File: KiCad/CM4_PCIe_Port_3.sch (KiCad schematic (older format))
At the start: 3 parts, among them J15 PCIe_x16

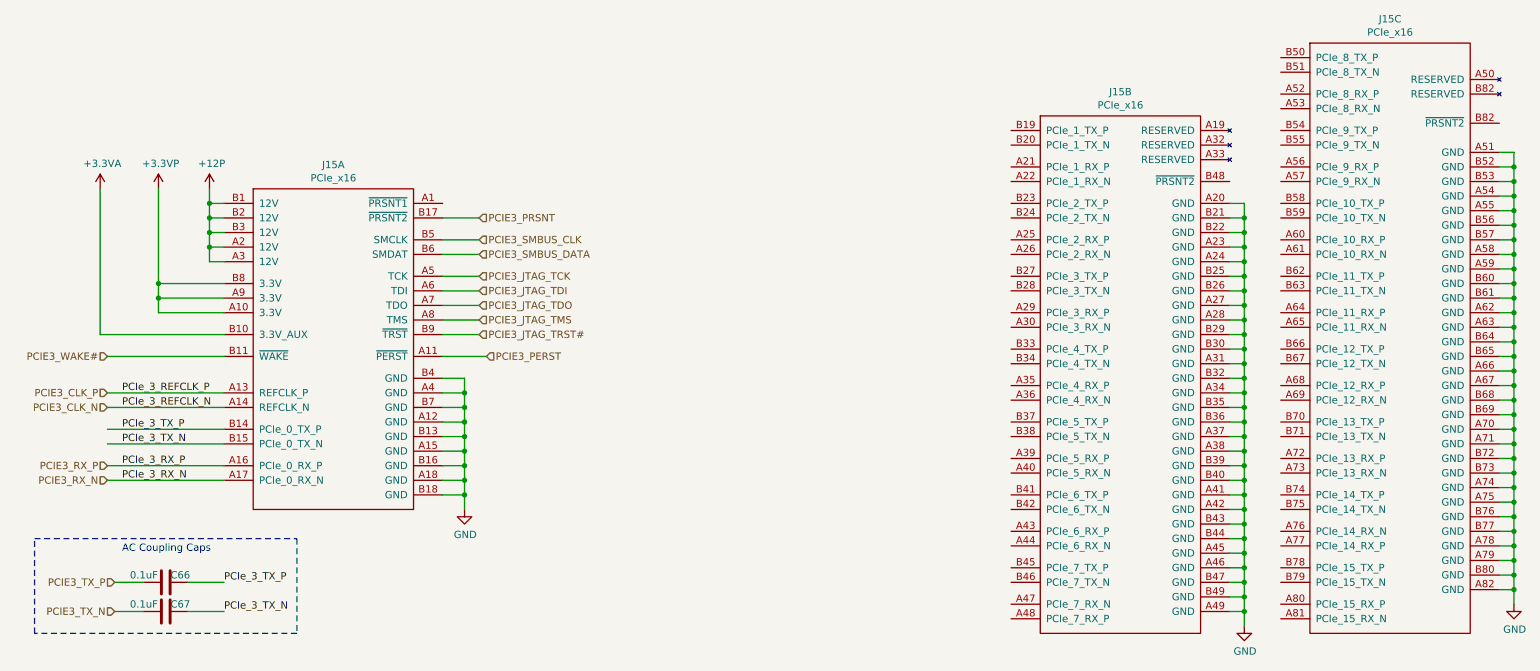
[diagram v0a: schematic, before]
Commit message: Tons of wiring and pin straps for PCI-e Switch
Also re-did some hierarchical labels for JTAG
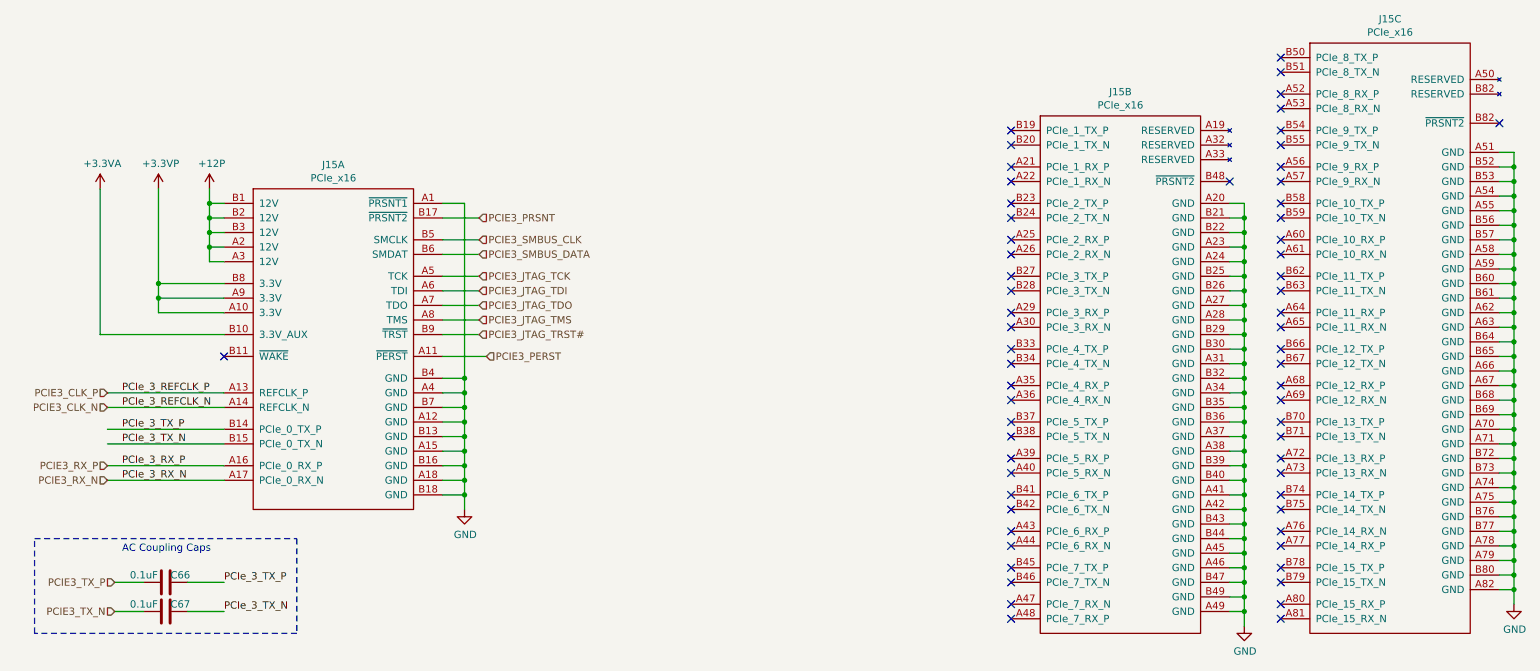
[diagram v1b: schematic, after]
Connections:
- net GND: now also J15.A1 (~PRSNT1)
- net PCIE3_WAKE#: no longer names the net of J15.B11 (~WAKE)
- no-connect marks 0 -> 63
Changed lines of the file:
@@
 PCIE3_SMBUS_DATA
-Wire Wire Line
-	2100 3700 1300 3700
-Text HLabel 1300 3700 0    50   Input ~ 0
-PCIE3_WAKE#
 Wire Wire Line
 	3600 3150 3850 3150
@@
 Text HLabel 3850 3550 2    50   Input ~ 0
 PCIE3_JTAG_TRST#
+NoConn ~ 9000 2500
+NoConn ~ 10850 2100
+NoConn ~ 9350 1650
+NoConn ~ 9350 1750
+NoConn ~ 9350 1900
+NoConn ~ 9350 2000
+NoConn ~ 9350 2150
+NoConn ~ 9350 2250
+NoConn ~ 9350 2400
+NoConn ~ 9350 2500
+NoConn ~ 9350 2650
+NoConn ~ 9350 2750
+NoConn ~ 9350 2900
+NoConn ~ 9350 3000
+NoConn ~ 9350 3150
+NoConn ~ 9350 3250
+NoConn ~ 9350 3400
+NoConn ~ 9350 3500
+NoConn ~ 9350 3650
+NoConn ~ 9350 3750
+NoConn ~ 9350 3900
+NoConn ~ 9350 4000
+NoConn ~ 9350 4150
+NoConn ~ 9350 4250
+NoConn ~ 9350 4400
+NoConn ~ 9350 4500
+NoConn ~ 9350 4650
+NoConn ~ 9350 4750
+NoConn ~ 9350 4900
+NoConn ~ 9350 5000
+NoConn ~ 9350 5150
+NoConn ~ 9350 5250
+NoConn ~ 9350 5400
+NoConn ~ 9350 5500
+NoConn ~ 7500 5500
+NoConn ~ 7500 5400
+NoConn ~ 7500 5250
+NoConn ~ 7500 5150
+NoConn ~ 7500 5000
+NoConn ~ 7500 4900
+NoConn ~ 7500 4750
+NoConn ~ 7500 4650
+NoConn ~ 7500 4500
+NoConn ~ 7500 4400
+NoConn ~ 7500 4250
+NoConn ~ 7500 4150
+NoConn ~ 7500 4000
+NoConn ~ 7500 3900
+NoConn ~ 7500 3750
+NoConn ~ 7500 3650
+NoConn ~ 7500 3500
+NoConn ~ 7500 3400
+NoConn ~ 7500 3250
+NoConn ~ 7500 3150
+NoConn ~ 7500 3000
+NoConn ~ 7500 2900
+NoConn ~ 7500 2750
+NoConn ~ 7500 2650
+NoConn ~ 7500 2500
+NoConn ~ 7500 2400
+NoConn ~ 7500 2250
+NoConn ~ 7500 2150
+Wire Wire Line
+	3600 2650 3750 2650
+Wire Wire Line
+	3750 2650 3750 3850
+Connection ~ 3750 3850
+NoConn ~ 2100 3700
 $EndSCHEMATC

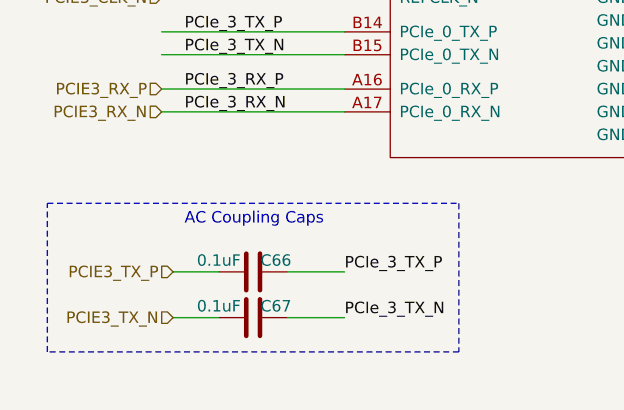
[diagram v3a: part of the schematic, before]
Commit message: Started picking passive components, overhauled library
Cleaned up a bunch of schematic library references.
Added datasheets, descriptions for a lot of existing parts.
Picked most capacitor parts, still a couple left.
Cleaned up a fair few footprint references.
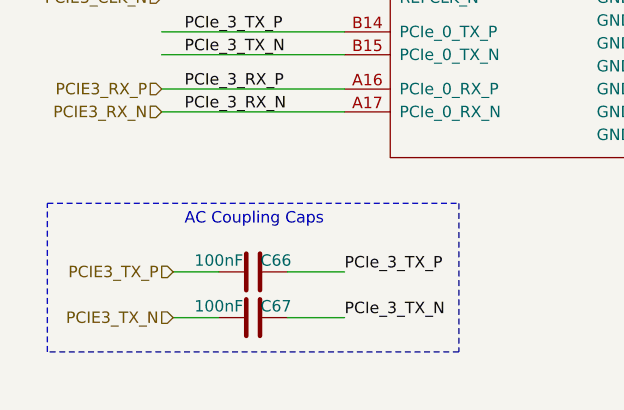
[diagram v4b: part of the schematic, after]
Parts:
- C66, C67: value 0.1uF -> 100nF; footprint (none) -> CM4_MATX:C_0402_1005Metric_Pad0.74x0.62mm_HandSolder; Description (none) -> 10V 0.1uF X5R 0402 20% Tol; Mfr. (none) -> AVX; Mfr. No (none) -> 0402ZD104MAT4A; Mouser Part Number (none) -> 581-0402ZD104MAT4A; Mouser Price/Stock (none) -> https://www.mouser.co.uk/ProductDetail/AVX/0402ZD104MAT4A/?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
- J15: Description (none) -> Amphenol FCI PCI-e x16 Connector 164 POS; Mfr. (none) -> Amphenol; Mfr. No (none) -> 10018783-10113TLF; Mouser Part Number (none) -> 649-18783-10113TLF; Mouser Price/Stock (none) -> https://www.mouser.co.uk/ProductDetail/Amphenol-FCI/1001878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
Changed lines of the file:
@@
 PCIE3_RX_P
 $Comp
-L power:GND #PWR?
+L CM4_MATX:GND #PWR?
 U 1 1 5FEB60E6
 P 3750 4750
@@
 PCIe_3_RX_N
 $Comp
-L power:+12P #PWR?
+L CM4_MATX:+12P #PWR?
 U 1 1 5FEB6112
 P 2000 2550
@@
 	2000 2650 2000 2550
 $Comp
-L power:+3.3VP #PWR?
+L CM4_MATX:+3.3VP #PWR?
 U 1 1 5FEB6126
 P 1650 2550
@@
 	1650 3200 1650 2550
 $Comp
-L power:+3.3VA #PWR?
+L CM4_MATX:+3.3VA #PWR?
 U 1 1 5FEB6134
 P 1250 2550
@@
 F 1 "PCIe_x16" H 2850 6324 50  0000 C CNN
 F 2 "CM4_MATX:10018783-10113TLF" H 1100 8800 50  0001 C CNN
-F 3 "" H 1100 8800 50  0001 C CNN
+F 3 "https://www.amphenol-icc.com/media/wysiwyg/files/documentation/datasheet/ssio/ssio_pcie_gen3.pdf" H 1100 8800 50  0001 C CNN
+F 4 "Amphenol FCI PCI-e x16 Connector 164 POS" H 2900 4400 50  0001 C CNN "Description"
+F 5 "649-18783-10113TLF" H 2900 4400 50  0001 C CNN "Mouser Part Number"
+F 6 "https://www.mouser.co.uk/ProductDetail/Amphenol-FCI/10018783-10113TLF/?qs=%2Fha2pyFadugRWVTwF3IyzEudyJIuC5mu1uxWW1BR%252B5VORiWMhxM3Zw%3D%3D" H 2900 4400 50  0001 C CNN "Mouser Price/Stock"
+F 7 "Amphenol" H 2900 4400 50  0001 C CNN "Mfr."
+F 8 "10018783-10113TLF" H 2900 4400 50  0001 C CNN "Mfr. No"
 	1    2900 4400
 	1    0    0    -1
@@
 F 1 "PCIe_x16" H 8250 5824 50  0000 C CNN
 F 2 "CM4_MATX:10018783-10113TLF" H 6450 8300 50  0001 C CNN
-F 3 "" H 6450 8300 50  0001 C CNN
+F 3 "https://www.amphenol-icc.com/media/wysiwyg/files/documentation/datasheet/ssio/ssio_pcie_gen3.pdf" H 6450 8300 50  0001 C CNN
+F 4 "Amphenol FCI PCI-e x16 Connector 164 POS" H 8250 3900 50  0001 C CNN "Description"
+F 5 "649-18783-10113TLF" H 8250 3900 50  0001 C CNN "Mouser Part Number"
+F 6 "https://www.mouser.co.uk/ProductDetail/Amphenol-FCI/10018783-10113TLF/?qs=%2Fha2pyFadugRWVTwF3IyzEudyJIuC5mu1uxWW1BR%252B5VORiWMhxM3Zw%3D%3D" H 8250 3900 50  0001 C CNN "Mouser Price/Stock"
+F 7 "Amphenol" H 8250 3900 50  0001 C CNN "Mfr."
+F 8 "10018783-10113TLF" H 8250 3900 50  0001 C CNN "Mfr. No"
 	2    8250 3900
 	1    0    0    -1
@@
 F 1 "PCIe_x16" H 10100 5324 50  0000 C CNN
 F 2 "CM4_MATX:10018783-10113TLF" H 8300 7800 50  0001 C CNN
-F 3 "" H 8300 7800 50  0001 C CNN
+F 3 "https://www.amphenol-icc.com/media/wysiwyg/files/documentation/datasheet/ssio/ssio_pcie_gen3.pdf" H 8300 7800 50  0001 C CNN
+F 4 "Amphenol FCI PCI-e x16 Connector 164 POS" H 10100 3400 50  0001 C CNN "Description"
+F 5 "649-18783-10113TLF" H 10100 3400 50  0001 C CNN "Mouser Part Number"
+F 6 "https://www.mouser.co.uk/ProductDetail/Amphenol-FCI/10018783-10113TLF/?qs=%2Fha2pyFadugRWVTwF3IyzEudyJIuC5mu1uxWW1BR%252B5VORiWMhxM3Zw%3D%3D" H 10100 3400 50  0001 C CNN "Mouser Price/Stock"
+F 7 "Amphenol" H 10100 3400 50  0001 C CNN "Mfr."
+F 8 "10018783-10113TLF" H 10100 3400 50  0001 C CNN "Mfr. No"
 	3    10100 3400
 	1    0    0    -1
@@
 	10950 5300 10950 5400
 $Comp
-L power:GND #PWR0193
+L CM4_MATX:GND #PWR0193
 U 1 1 601661E8
 P 10950 5400
@@
 $EndComp
 $Comp
-L power:GND #PWR0194
+L CM4_MATX:GND #PWR0194
 U 1 1 60166A1C
 P 9100 5550
@@
 AR Path="/5FFBC089/5FFBFF34/5FF316D6" Ref="C67"  Part="1"
 F 0 "C67" V 1650 5550 50  0000 C CNN
-F 1 "0.1uF" V 1650 5300 50  0000 C CNN
-F 2 "" H 1738 5300 50  0001 C CNN
-F 3 "~" H 1700 5450 50  0001 C CNN
+F 1 "100nF" V 1650 5300 50  0000 C CNN
+F 2 "CM4_MATX:C_0402_1005Metric_Pad0.74x0.62mm_HandSolder" H 1738 5300 50  0001 C CNN
+F 3 "https://www.mouser.co.uk/datasheet/2/40/cx5r-776519.pdf" H 1700 5450 50  0001 C CNN
+F 4 "581-0402ZD104MAT4A" H 1700 5450 50  0001 C CNN "Mouser Part Number"
+F 5 "https://www.mouser.co.uk/ProductDetail/AVX/0402ZD104MAT4A/?qs=sGAEpiMZZMvsSlwiRhF8qud6rLLpfNdE%2FYSoyEGdkn4%3D" H 1700 5450 50  0001 C CNN "Mouser Price/Stock"
+F 6 "AVX" H 1700 5450 50  0001 C CNN "Mfr."
+F 7 "0402ZD104MAT4A" H 1700 5450 50  0001 C CNN "Mfr. No"
+F 8 "10V 0.1uF X5R 0402 20% Tol" H 1700 5450 50  0001 C CNN "Description"
 	1    1700 5450
 	0    1    1    0
@@
 AR Path="/5FFBC089/5FFBFF34/5FF316DC" Ref="C66"  Part="1"
 F 0 "C66" V 1750 5150 50  0000 C CNN
-F 1 "0.1uF" V 1750 5400 50  0000 C CNN
-F 2 "" H 1738 5100 50  0001 C CNN
-F 3 "~" H 1700 5250 50  0001 C CNN
+F 1 "100nF" V 1750 5400 50  0000 C CNN
+F 2 "CM4_MATX:C_0402_1005Metric_Pad0.74x0.62mm_HandSolder" H 1738 5100 50  0001 C CNN
+F 3 "https://www.mouser.co.uk/datasheet/2/40/cx5r-776519.pdf" H 1700 5250 50  0001 C CNN
+F 4 "581-0402ZD104MAT4A" H 1700 5250 50  0001 C CNN "Mouser Part Number"
+F 5 "https://www.mouser.co.uk/ProductDetail/AVX/0402ZD104MAT4A/?qs=sGAEpiMZZMvsSlwiRhF8qud6rLLpfNdE%2FYSoyEGdkn4%3D" H 1700 5250 50  0001 C CNN "Mouser Price/Stock"
+F 6 "AVX" H 1700 5250 50  0001 C CNN "Mfr."
+F 7 "0402ZD104MAT4A" H 1700 5250 50  0001 C CNN "Mfr. No"
+F 8 "10V 0.1uF X5R 0402 20% Tol" H 1700 5250 50  0001 C CNN "Description"
 	1    1700 5250
 	0    -1   -1   0

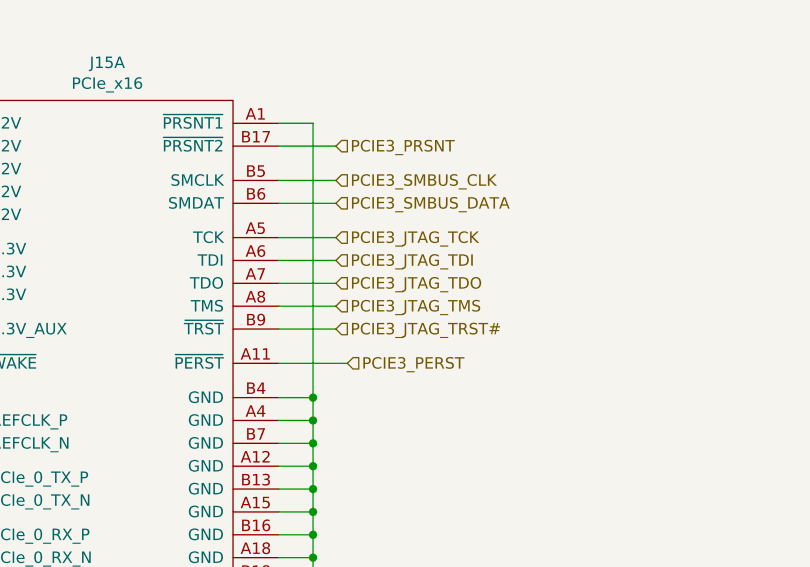
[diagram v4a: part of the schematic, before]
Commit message: Imported new components to the PCB and moved some components
Updated PDFs and added two new board layers. One for ground and a second for power (voltage to be decided)
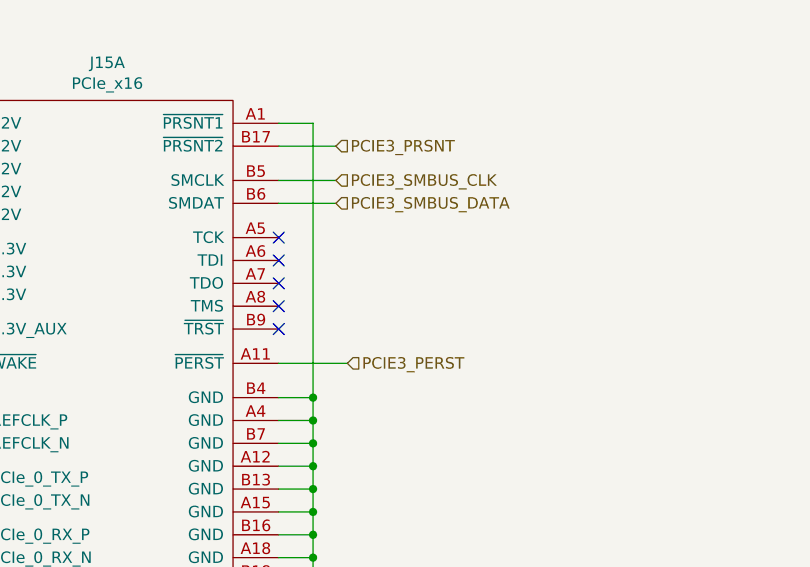
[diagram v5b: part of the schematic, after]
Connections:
- net PCIE3_JTAG_TCK: no longer names the net of J15.A5 (TCK)
- net PCIE3_JTAG_TDI: no longer names the net of J15.A6 (TDI)
- net PCIE3_JTAG_TDO: no longer names the net of J15.A7 (TDO)
- net PCIE3_JTAG_TMS: no longer names the net of J15.A8 (TMS)
- net PCIE3_JTAG_TRST#: no longer names the net of J15.B9 (~TRST)
- no-connect marks 63 -> 68
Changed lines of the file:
@@
 $Descr A4 11693 8268
 encoding utf-8
-Sheet 14 16
+Sheet 13 15
 Title ""
 Date "2021-02-08"
@@
 Text HLabel 3850 3000 2    50   Input ~ 0
 PCIE3_SMBUS_DATA
-Wire Wire Line
-	3600 3150 3850 3150
-Wire Wire Line
-	3600 3250 3850 3250
-Wire Wire Line
-	3600 3350 3850 3350
-Wire Wire Line
-	3600 3450 3850 3450
-Wire Wire Line
-	3600 3550 3850 3550
-Text HLabel 3850 3150 2    50   Input ~ 0
-PCIE3_JTAG_TCK
-Text HLabel 3850 3250 2    50   Input ~ 0
-PCIE3_JTAG_TDI
-Text HLabel 3850 3350 2    50   Input ~ 0
-PCIE3_JTAG_TDO
-Text HLabel 3850 3450 2    50   Input ~ 0
-PCIE3_JTAG_TMS
-Text HLabel 3850 3550 2    50   Input ~ 0
-PCIE3_JTAG_TRST#
 NoConn ~ 9000 2500
 NoConn ~ 10850 2100
@@
 Connection ~ 3750 3850
 NoConn ~ 2100 3700
+NoConn ~ 3600 3150
+NoConn ~ 3600 3250
+NoConn ~ 3600 3350
+NoConn ~ 3600 3450
+NoConn ~ 3600 3550
 $EndSCHEMATC
